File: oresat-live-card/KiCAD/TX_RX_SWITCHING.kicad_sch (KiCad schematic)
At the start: 40 parts, among them J11 2X1_TH_JUMPER, J15 2X1_TH_JUMPER, U23 SN74LVC1G32QDBVRQ1, U24 LTC6994-1, U25 LTC6994-1, U26 SN74LV1T34, U32 SN74LV1T34, U34 QPC1022, U35 SN74LVC1G32QDBVRQ1, U36 QPC1022, U6 NC7SVU04P5X

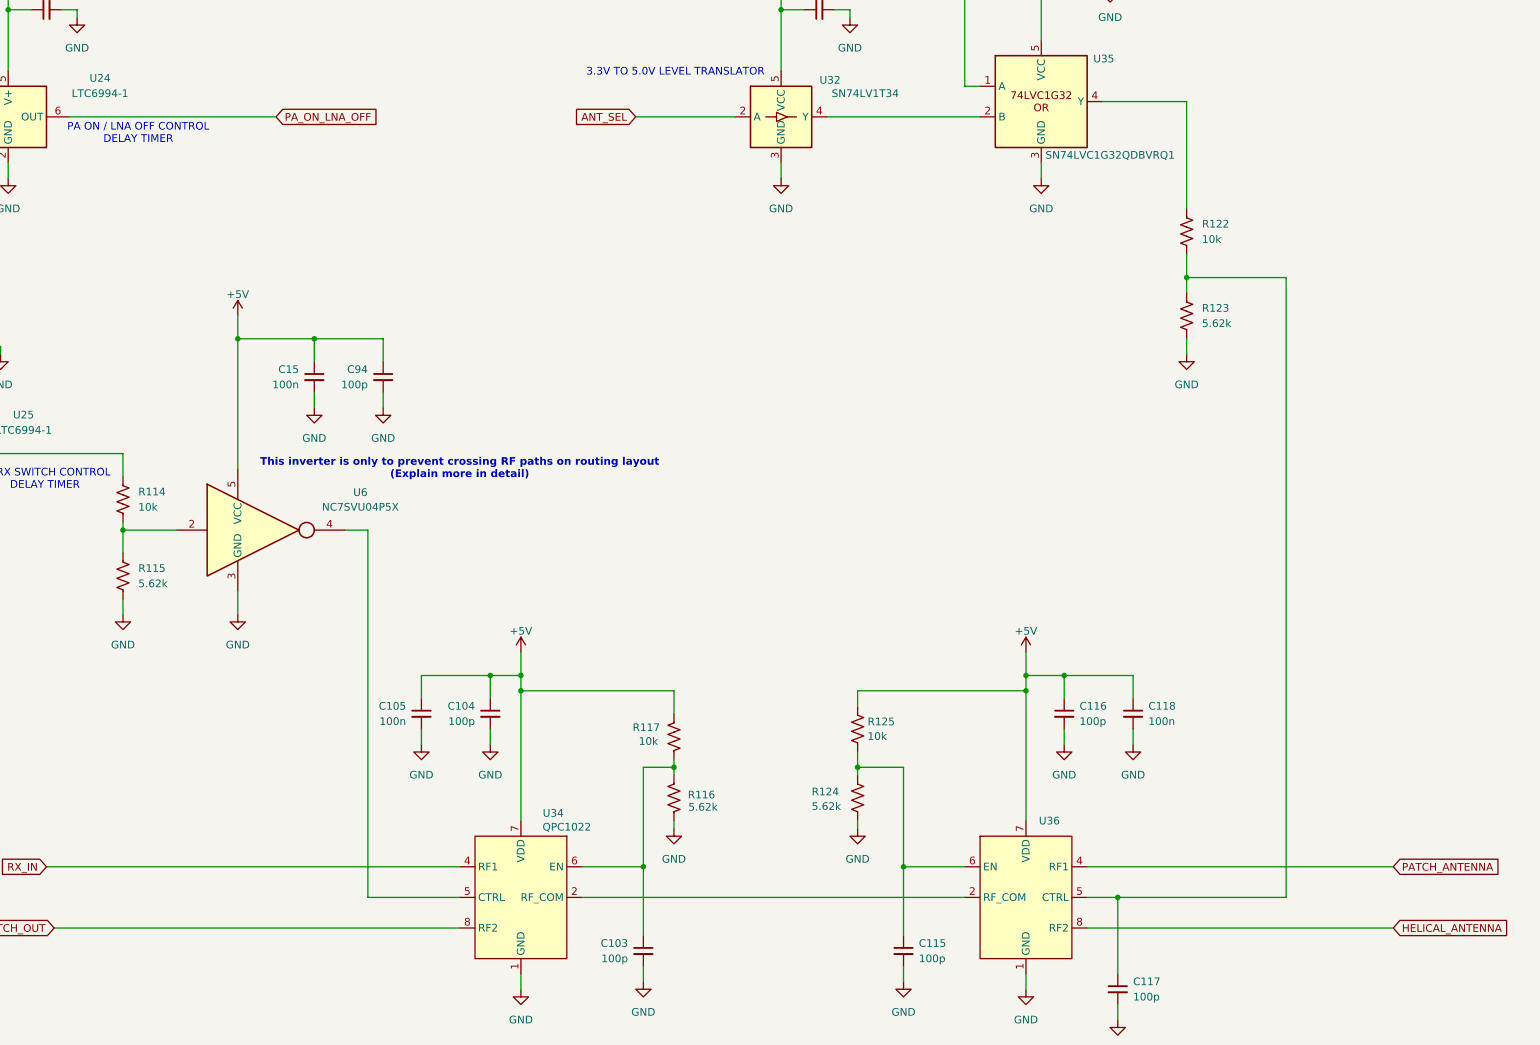
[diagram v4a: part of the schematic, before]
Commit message: initial routing pass completed, moved R144 and R155 to output of U6.
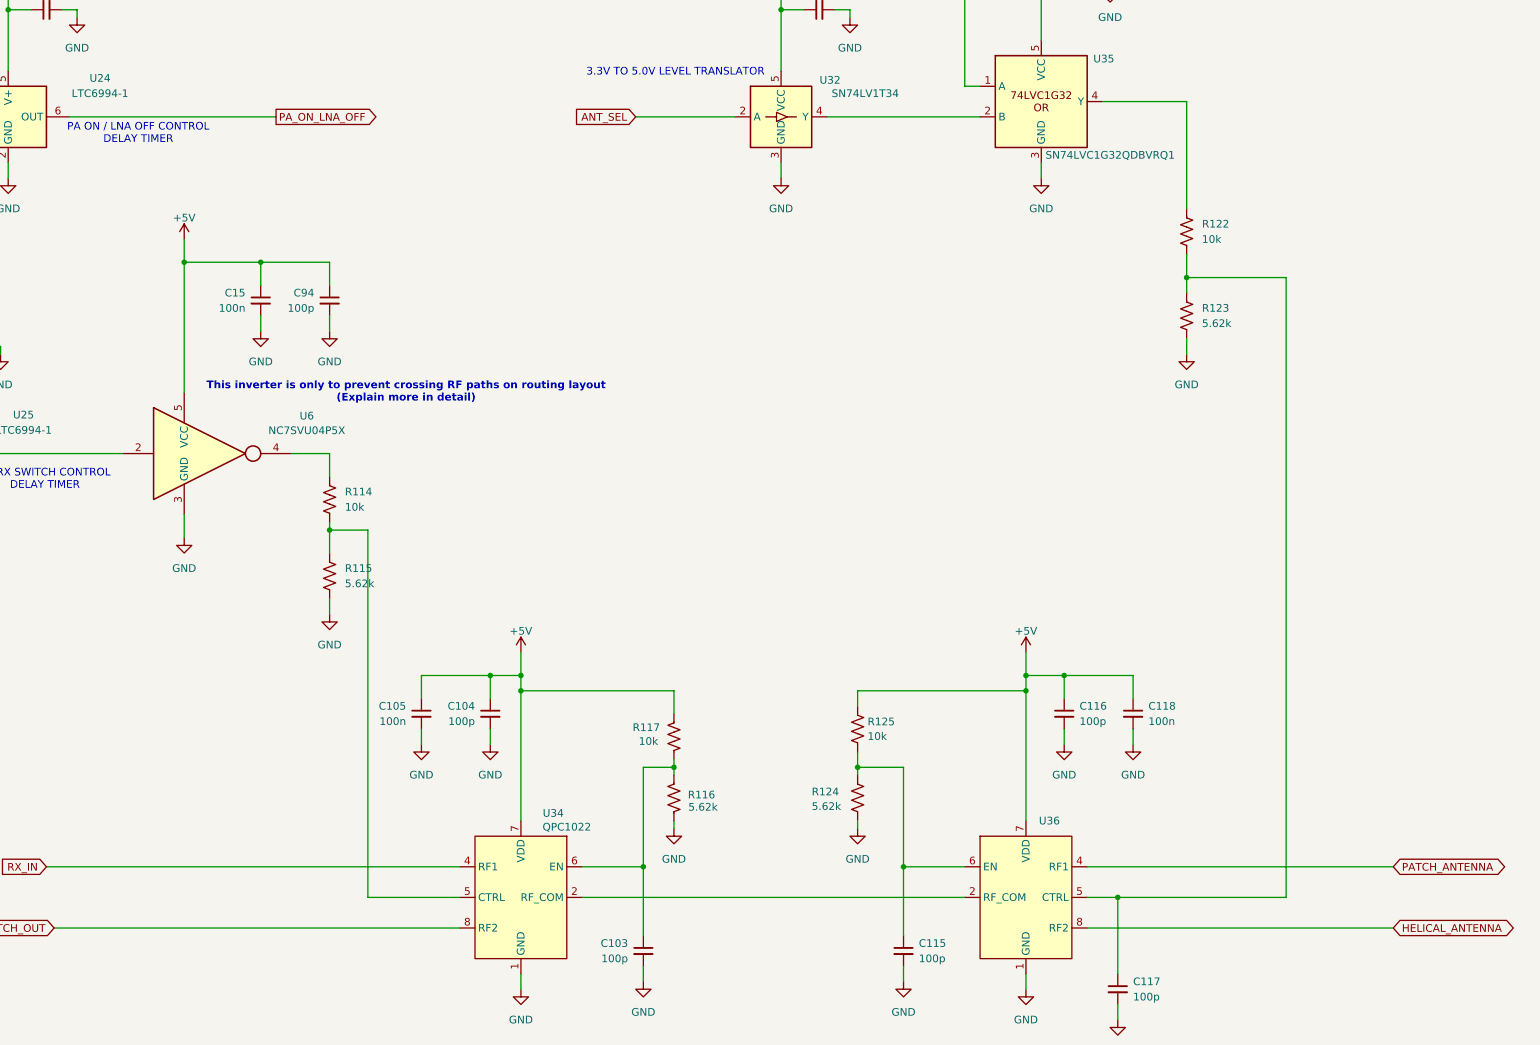
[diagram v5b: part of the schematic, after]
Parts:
- C105, C15, C86, R116, R117, R87: footprint Resistor_SMD:R_0603_1608Metric -> oresat-passives:0402-C
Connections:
- net at R114.1, R115.1: now also U34.5 (CTRL); no longer U6.2
- net at U6.4: now also R114.2; no longer U34.5 (CTRL)
- net at U25.6 (OUT): now also U6.2; no longer R114.2
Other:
- moved on the sheet: C15, C94, R114, R115, U6

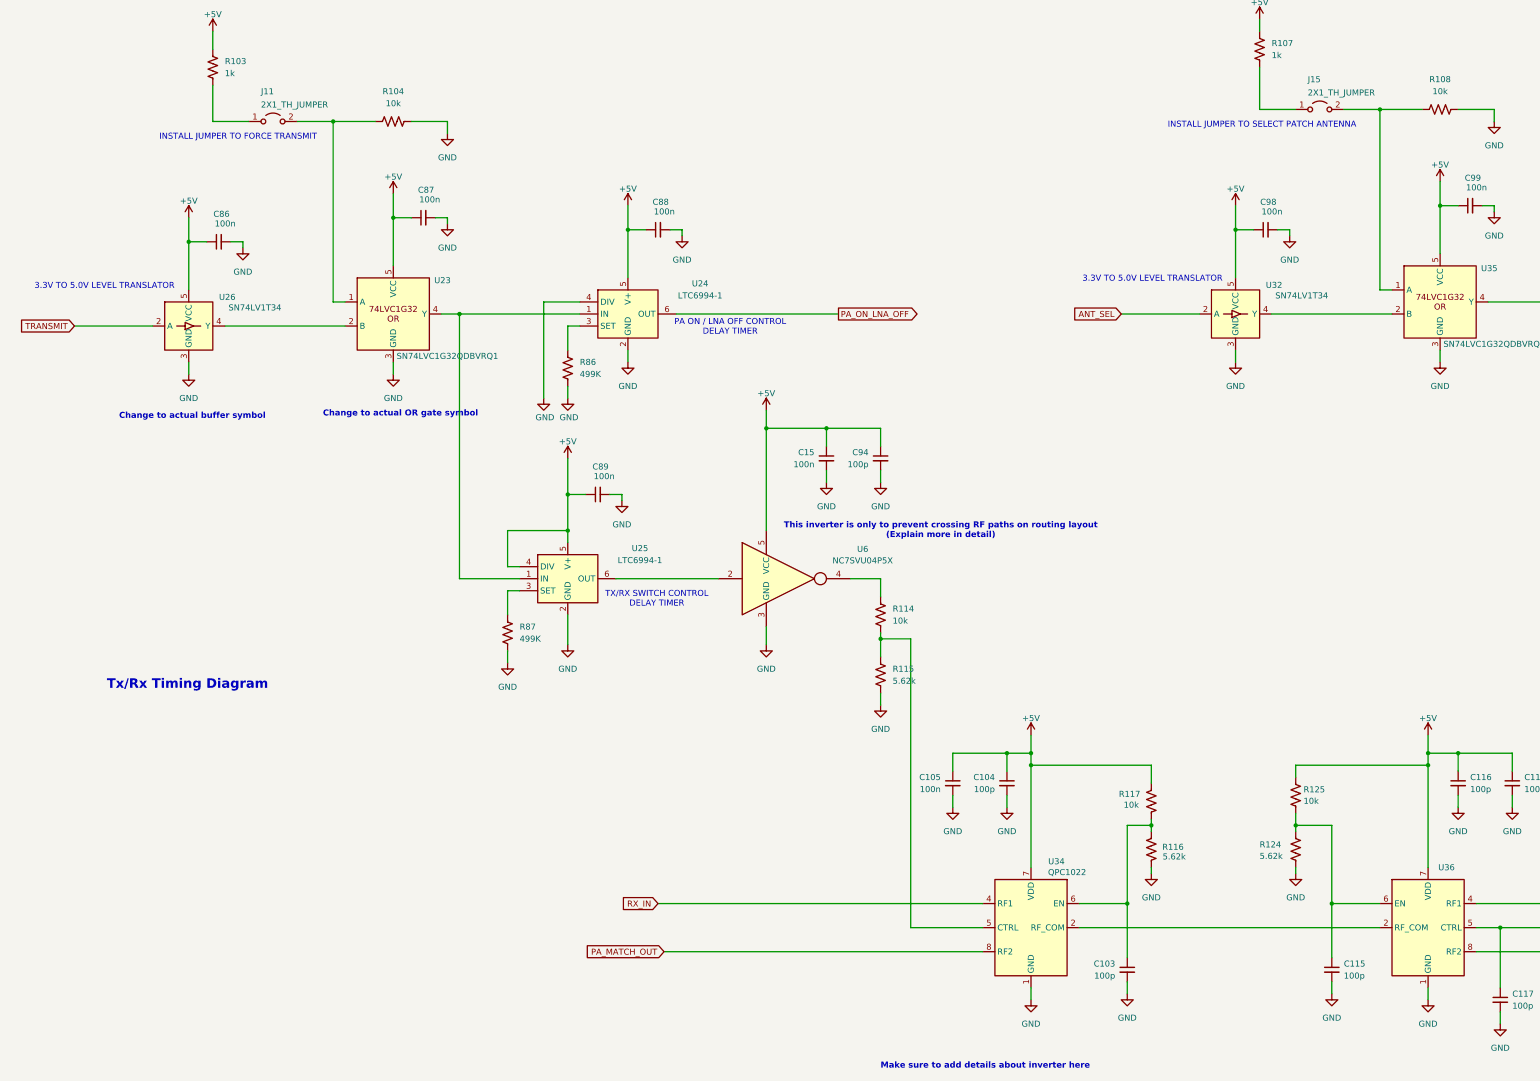
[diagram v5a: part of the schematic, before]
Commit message: Fixed schematic symbolrs, add notes about control logic, fixed RF path and teardrops, removed 1.1V power LED
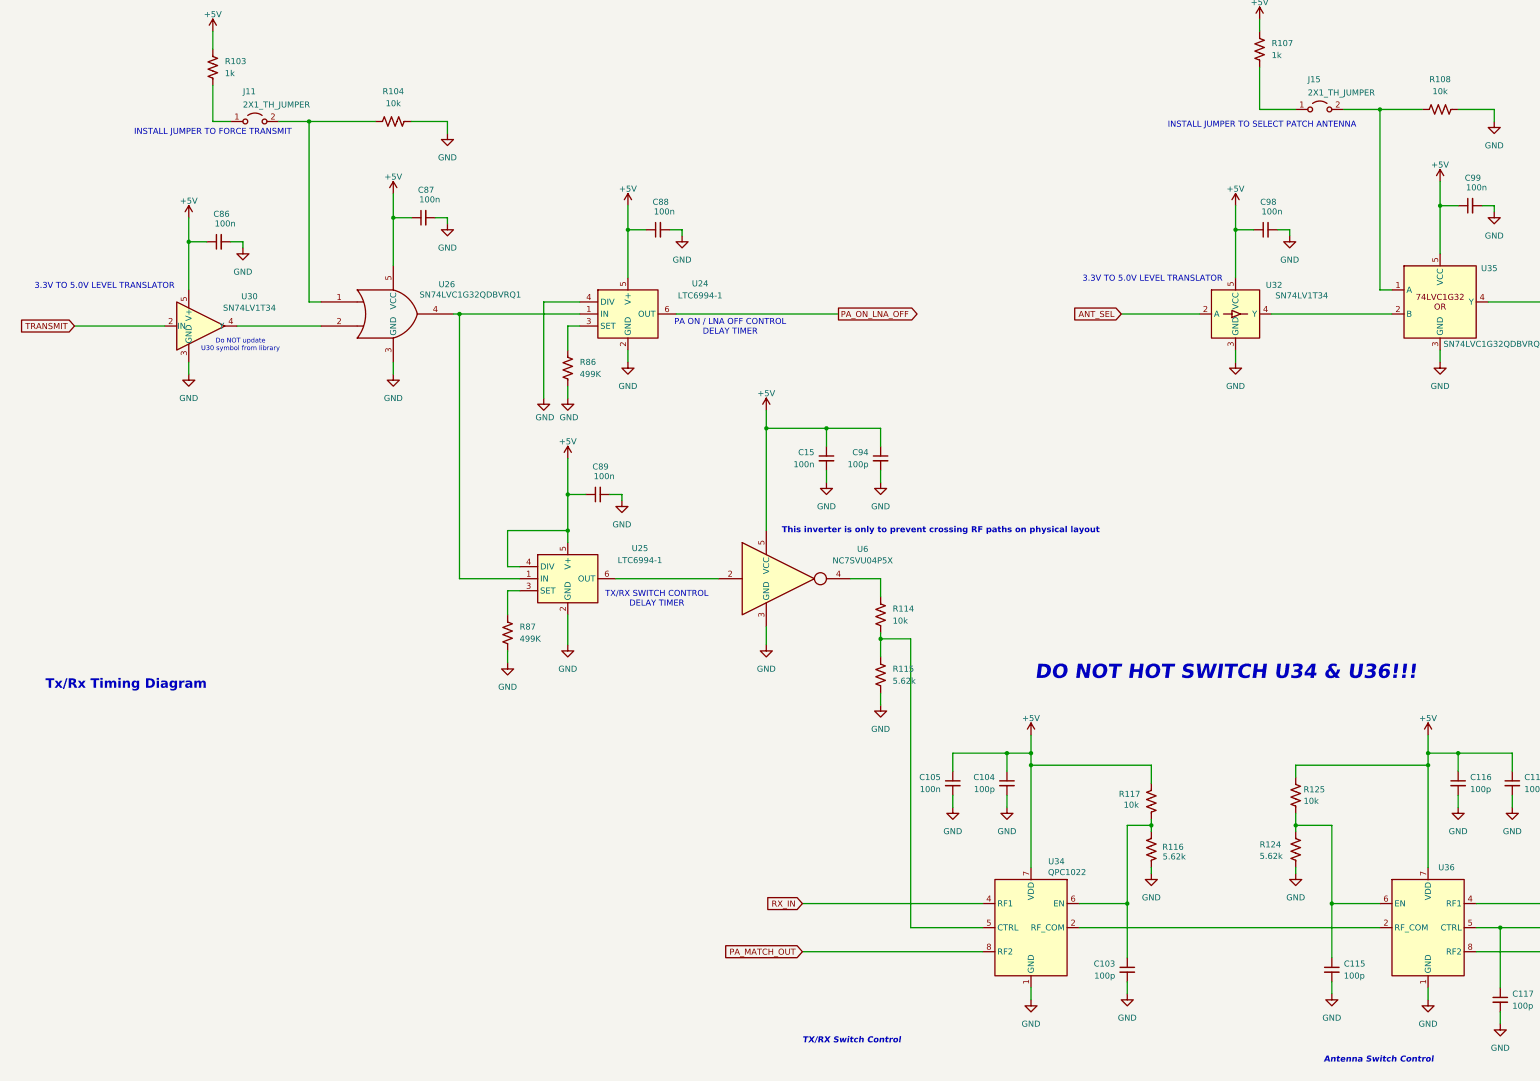
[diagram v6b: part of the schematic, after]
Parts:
- removed U23: SN74LVC1G32QDBVRQ1, Package_TO_SOT_SMD:SOT-23-5, symbol oresat-ics:SN74LVC1G32QDBVRQ1
- removed U26: SN74LV1T34, Package_TO_SOT_SMD:SOT-353_SC-70-5, symbol Logic_LevelTranslator:SN74LV1T34DCK
- added U26: SN74LVC1G32QDBVRQ1, Package_TO_SOT_SMD:SOT-23-5, symbol 74xGxx:74LVC1G32
- added U30: SN74LV1T34, Package_TO_SOT_SMD:SOT-23-5, symbol Amplifier_Buffer:LM6321H
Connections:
- net +5V: now also U26.5 (VCC), U30.5 (V+)
- net GND: now also U26.3 (GND), U30.3 (GND)
- net TRANSMIT: now also U30.2 (IN)
- net at J11.2 (B), R104.1: now also U26.1
- net at U24.1 (IN), U25.1 (IN): now also U26.4
- new net: U26.2, U30.4 (Y)
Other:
- note added: "Antenna Switch Control"
- note added: "DO NOT HOT SWITCH U34 & U36!!!"
- note added: "Do NOT update U30 symbol from library"
- note added: "TX/RX Switch Control"
- note added: "This inverter is only to prevent crossing RF paths on physical layout"
- note removed: "Change to actual OR gate symbol"
- note removed: "Change to actual buffer symbol"
- note removed: "Make sure to add details about inverter here"
- note removed: "This inverter is only to prevent crossing RF paths on routing layout (Explain more in detail)"
- moved on the sheet: J11

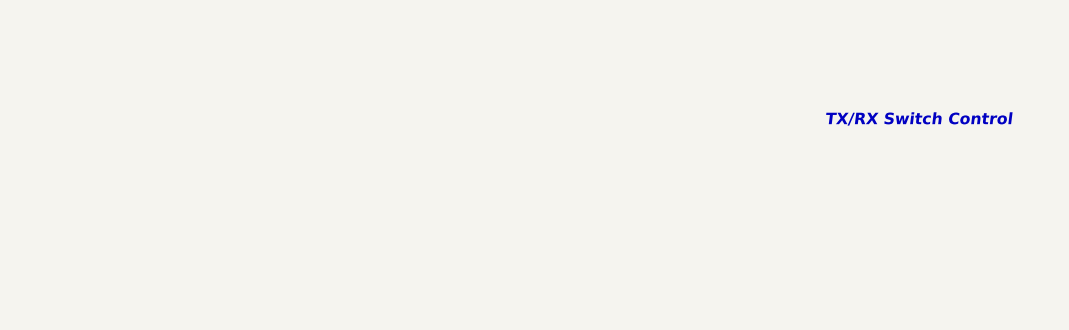
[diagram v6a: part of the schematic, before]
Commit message: CLeaned up main connector, page names to be consistent with Octavo designs, sanity checks.
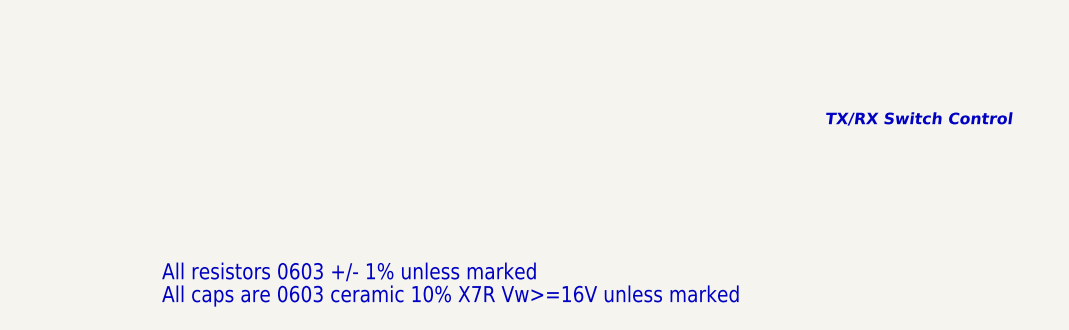
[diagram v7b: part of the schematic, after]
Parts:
- C103, C104, C105, C115, C116, C117, C118, C15, C86, C87, C88, C89, C94, C98, C99, R104, R108, R114, R115, R116, R117, R122, R123, R124, R125, R86, R87, U30, U32, U34, U36: DIS (none) -> DigiKey; Distributor DigiKey -> (none)
- R103, R107: DIS (none) -> DigiKey; Distributor DigiKey -> (none); MFR Panasonic -> Panasonic
- U24, U25: Distributor Mouser -> (none)
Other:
- note added: "All caps are 0603 ceramic 10% X7R Vw>=16V unless marked"
- note added: "All resistors 0603 +/- 1% unless marked"
- title: Oresat DxWifi Card -> Oresat Live Card
